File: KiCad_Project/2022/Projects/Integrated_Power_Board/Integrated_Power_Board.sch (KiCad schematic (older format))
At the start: 21 parts, among them J1 Conn_01x02, J2 Conn_01x02, J3 Conn_01x02, J4 Conn_01x02, J5 Conn_01x02, SW1 Switch_SW_SPST, SW2 SW_SPST, U1 OKL-T_6-W12N-C

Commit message: Kicadプロジェクトの整理
ファイルについて
各基板のプロジェクト・ライブラリ・PDF・DXF・自動配線用・発注ファイル
に分けました。
またライブラリのインポートに際してプロフェクトからの相対パスに変更したため環境を変更しても編集することができます。
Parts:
- BT1: footprint (none) -> Connector_JST:JST_VH_B2P-VH-B_1x02_P3.96mm_Vertical
- F1: footprint (none) -> herakuresu2022:fuse_socket
- MES1: footprint (none) -> herakuresu2022:voltage_counter
- SW1: symbol Integrated_Power_Board-cache:Switch_SW_SPST -> Integrated_Power_Board-rescue:Switch_SW_SPST-Integrated_Power_Board-cache
- SW2: footprint (none) -> herakuresu2022:2MS1T2B4M2QES
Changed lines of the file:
@@
 F 0 "SW2" V 6054 2948 50  0000 L CNN
 F 1 "SW_SPST" V 6145 2948 50  0000 L CNN
-F 2 "" H 6100 2850 50  0001 C CNN
+F 2 "herakuresu2022:2MS1T2B4M2QES" H 6100 2850 50  0001 C CNN
 F 3 "~" H 6100 2850 50  0001 C CNN
 	1    6100 2850
@@
 F 0 "BT1" H 1808 2596 50  0000 L CNN
 F 1 "Battery" H 1808 2505 50  0000 L CNN
-F 2 "" V 1700 2610 50  0001 C CNN
+F 2 "Connector_JST:JST_VH_B2P-VH-B_1x02_P3.96mm_Vertical" V 1700 2610 50  0001 C CNN
 F 3 "~" V 1700 2610 50  0001 C CNN
 	1    1700 2550
@@
 F 0 "F1" V 1803 2350 50  0000 C CNN
 F 1 "Fuse" V 1894 2350 50  0000 C CNN
-F 2 "" V 1930 2350 50  0001 C CNN
+F 2 "herakuresu2022:fuse_socket" V 1930 2350 50  0001 C CNN
 F 3 "~" H 2000 2350 50  0001 C CNN
 	1    2000 2350
@@
 $EndComp
 $Comp
-L Integrated_Power_Board-cache:Switch_SW_SPST SW1
+L Integrated_Power_Board-rescue:Switch_SW_SPST-Integrated_Power_Board-cache SW1
 U 1 1 61EC8A2A
 P 3300 2350
@@
 F 0 "MES1" H 3000 2450 50  0000 L CNN
 F 1 "Voltmeter_DC" H 2650 2250 50  0000 L CNN
-F 2 "" V 2900 2650 50  0001 C CNN
+F 2 "herakuresu2022:voltage_counter" V 2900 2650 50  0001 C CNN
 F 3 "~" V 2900 2650 50  0001 C CNN
 	1    2900 2550

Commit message: 電源系の設計の完了
ATtinyを使って電圧を測定してシリアルでメインマイコンに送信します
レベル変換についてはまだ考えてない
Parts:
- removed SW1: Switch_SW_SPST, symbol Integrated_Power_Board-rescue:Switch_SW_SPST-Integrated_Power_Board-cache
- added C1: CP, symbol Device:CP
- added D1: D_Shockley, symbol Device:D_Shockley
- added D2: LED, symbol Device:LED
- added J1: Conn_01x02, symbol Connector_Generic:Conn_01x02
- added R1, R2, R3: R, symbol Device:R
- added SW1: SW_SPST, herakuresu2022:2MS1T2B4M2QES, symbol Switch:SW_SPST
- added U1: ATtiny85-20PU, Package_DIP:DIP-8_W7.62mm, symbol MCU_Microchip_ATtiny:ATtiny85-20PU
- renumbered C1 to C2, C2 to C3, C3 to C4, D2 to D3, J1 to J2, J2 to J3, J3 to J4, J4 to J5, J5 to J6, R1 to R4, R2 to R5, R3 to R6, U1 to U2
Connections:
- net labels added: RX, TX
- wire segments 44 -> 61
- no-connect marks 1 -> 3
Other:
- moved on the sheet: BT1, F1, J2, J3, J4, MES1

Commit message: 進捗
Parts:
- C1, C2: footprint (none) -> Capacitor_THT:C_Radial_D16.0mm_H25.0mm_P7.50mm
- C3, C4: footprint (none) -> Capacitor_THT:C_Disc_D3.0mm_W1.6mm_P2.50mm
- D1: footprint (none) -> Diode_THT:D_DO-201AD_P12.70mm_Horizontal
- D2: footprint (none) -> LED_THT:LED_D3.0mm_Clear
- D3: footprint (none) -> Diode_THT:D_DO-41_SOD81_P7.62mm_Horizontal
- F1: footprint herakuresu2022:fuse_socket -> Library:fuse_socket
- FL1: footprint BNX016-01:FIL_BNX016-01 -> Library:FIL_BNX016-01
- J1: footprint (none) -> Connector_JST:JST_XH_B2B-XH-A_1x02_P2.50mm_Vertical
- MES1: footprint herakuresu2022:voltage_counter -> Library:voltage_counter
- R1, R2, R3, R4, R5, R6: footprint (none) -> Resistor_THT:R_Axial_DIN0207_L6.3mm_D2.5mm_P7.62mm_Horizontal
- RV2: footprint (none) -> Potentiometer_THT:Potentiometer_Bourns_3296W_Vertical
- SW1: footprint herakuresu2022:2MS1T2B4M2QES -> (none)
- SW2: footprint herakuresu2022:2MS1T2B4M2QES -> Library:toggleswitch
- U2: footprint OKL-T_6-W12N-C:DCDC-murata-6A -> Library:DCDC-murata-6A
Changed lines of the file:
@@
 F 0 "FL1" H 4500 2775 50  0000 C CNN
 F 1 "BNX025" H 4500 2684 50  0000 C CNN
-F 2 "BNX016-01:FIL_BNX016-01" H 4500 2250 50  0001 C CNN
+F 2 "Library:FIL_BNX016-01" H 4500 2250 50  0001 C CNN
 F 3 "https://www.murata.com/en-us/products/productdetail.aspx?cate=luNoiseSupprFilteBlockType&partno=BNX025H01%23" V 4475 2425 50  0001 C CNN
 	1    4500 2450
@@
 F 0 "C2" H 5418 2546 50  0000 L CNN
 F 1 "CP" H 5418 2455 50  0000 L CNN
-F 2 "" H 5338 2350 50  0001 C CNN
+F 2 "Capacitor_THT:C_Radial_D16.0mm_H25.0mm_P7.50mm" H 5338 2350 50  0001 C CNN
 F 3 "~" H 5300 2500 50  0001 C CNN
 	1    5300 2500
@@
 F 0 "D3" H 9350 2133 50  0000 C CNN
 F 1 "D" H 9350 2224 50  0000 C CNN
-F 2 "" H 9350 2350 50  0001 C CNN
+F 2 "Diode_THT:D_DO-41_SOD81_P7.62mm_Horizontal" H 9350 2350 50  0001 C CNN
 F 3 "~" H 9350 2350 50  0001 C CNN
 	1    9350 2350
@@
 F 0 "C4" H 8965 2696 50  0000 L CNN
 F 1 "C" H 8965 2605 50  0000 L CNN
-F 2 "" H 8888 2500 50  0001 C CNN
+F 2 "Capacitor_THT:C_Disc_D3.0mm_W1.6mm_P2.50mm" H 8888 2500 50  0001 C CNN
 F 3 "~" H 8850 2650 50  0001 C CNN
 	1    8850 2650
@@
 F 0 "C3" H 6015 2546 50  0000 L CNN
 F 1 "C" H 6015 2455 50  0000 L CNN
-F 2 "" H 5938 2350 50  0001 C CNN
+F 2 "Capacitor_THT:C_Disc_D3.0mm_W1.6mm_P2.50mm" H 5938 2350 50  0001 C CNN
 F 3 "~" H 5900 2500 50  0001 C CNN
 	1    5900 2500
@@
 F 0 "R4" H 6320 2596 50  0000 L CNN
 F 1 "R" H 6320 2505 50  0000 L CNN
-F 2 "" V 6180 2550 50  0001 C CNN
+F 2 "Resistor_THT:R_Axial_DIN0207_L6.3mm_D2.5mm_P7.62mm_Horizontal" V 6180 2550 50  0001 C CNN
 F 3 "~" H 6250 2550 50  0001 C CNN
 	1    6250 2550
@@
 F 0 "R6" H 9220 2696 50  0000 L CNN
 F 1 "R" H 9220 2605 50  0000 L CNN
-F 2 "" V 9080 2650 50  0001 C CNN
+F 2 "Resistor_THT:R_Axial_DIN0207_L6.3mm_D2.5mm_P7.62mm_Horizontal" V 9080 2650 50  0001 C CNN
 F 3 "~" H 9150 2650 50  0001 C CNN
 	1    9150 2650
@@
 F 0 "RV2" V 8175 2725 50  0000 R CNN
 F 1 "R_POT_TRIM_US" V 8450 2950 50  0000 R CNN
-F 2 "" H 8250 2650 50  0001 C CNN
+F 2 "Potentiometer_THT:Potentiometer_Bourns_3296W_Vertical" H 8250 2650 50  0001 C CNN
 F 3 "~" H 8250 2650 50  0001 C CNN
 	1    8250 2650
@@
 F 0 "R5" H 8670 2846 50  0000 L CNN
 F 1 "R" H 8670 2755 50  0000 L CNN
-F 2 "" V 8530 2800 50  0001 C CNN
+F 2 "Resistor_THT:R_Axial_DIN0207_L6.3mm_D2.5mm_P7.62mm_Horizontal" V 8530 2800 50  0001 C CNN
 F 3 "~" H 8600 2800 50  0001 C CNN
 	1    8600 2800
@@
 F 0 "F1" V 1678 2350 50  0000 C CNN
 F 1 "Fuse" V 1769 2350 50  0000 C CNN
-F 2 "herakuresu2022:fuse_socket" V 1805 2350 50  0001 C CNN
+F 2 "Library:fuse_socket" V 1805 2350 50  0001 C CNN
 F 3 "~" H 1875 2350 50  0001 C CNN
 	1    1875 2350
@@
 F 0 "MES1" H 2875 2450 50  0000 L CNN
 F 1 "Voltmeter_DC" H 2525 2250 50  0000 L CNN
-F 2 "herakuresu2022:voltage_counter" V 2775 2650 50  0001 C CNN
+F 2 "Library:voltage_counter" V 2775 2650 50  0001 C CNN
 F 3 "~" V 2775 2650 50  0001 C CNN
 	1    2775 2550
@@
 F 0 "SW2" V 6054 2948 50  0000 L CNN
 F 1 "SW_SPST" V 6145 2948 50  0000 L CNN
-F 2 "herakuresu2022:2MS1T2B4M2QES" H 6100 2850 50  0001 C CNN
+F 2 "Library:toggleswitch" H 6100 2850 50  0001 C CNN
 F 3 "~" H 6100 2850 50  0001 C CNN
 	1    6100 2850
@@
 F 0 "U2" H 7200 3215 50  0000 C CNN
 F 1 "OKL-T_6-W12N-C" H 7200 3124 50  0000 C CNN
-F 2 "OKL-T_6-W12N-C:DCDC-murata-6A" H 6750 3100 50  0001 L BNN
+F 2 "Library:DCDC-murata-6A" H 6750 3100 50  0001 L BNN
 F 3 "" H 7200 2650 50  0001 L BNN
 	1    7200 2650
@@
 F 0 "SW1" V 3129 2448 50  0000 L CNN
 F 1 "SW_SPST" V 3220 2448 50  0000 L CNN
-F 2 "herakuresu2022:2MS1T2B4M2QES" H 3175 2350 50  0001 C CNN
+F 2 "" H 3175 2350 50  0001 C CNN
 F 3 "~" H 3175 2350 50  0001 C CNN
 	1    3175 2350
@@
 F 0 "D1" V 2054 2630 50  0000 L CNN
 F 1 "D_Shockley" V 2145 2630 50  0000 L CNN
-F 2 "" H 2100 2550 50  0001 C CNN
+F 2 "Diode_THT:D_DO-201AD_P12.70mm_Horizontal" H 2100 2550 50  0001 C CNN
 F 3 "~" H 2100 2550 50  0001 C CNN
 	1    2100 2550
@@
 F 0 "C1" H 3593 2596 50  0000 L CNN
 F 1 "CP" H 3593 2505 50  0000 L CNN
-F 2 "" H 3513 2400 50  0001 C CNN
+F 2 "Capacitor_THT:C_Radial_D16.0mm_H25.0mm_P7.50mm" H 3513 2400 50  0001 C CNN
 F 3 "~" H 3475 2550 50  0001 C CNN
 	1    3475 2550
@@
 F 0 "R2" H 4195 3821 50  0000 L CNN
 F 1 "R" H 4195 3730 50  0000 L CNN
-F 2 "" V 4055 3775 50  0001 C CNN
+F 2 "Resistor_THT:R_Axial_DIN0207_L6.3mm_D2.5mm_P7.62mm_Horizontal" V 4055 3775 50  0001 C CNN
 F 3 "~" H 4125 3775 50  0001 C CNN
 	1    4125 3775
@@
 F 0 "R3" H 4195 4121 50  0000 L CNN
 F 1 "R" H 4195 4030 50  0000 L CNN
-F 2 "" V 4055 4075 50  0001 C CNN
+F 2 "Resistor_THT:R_Axial_DIN0207_L6.3mm_D2.5mm_P7.62mm_Horizontal" V 4055 4075 50  0001 C CNN
 F 3 "~" H 4125 4075 50  0001 C CNN
 	1    4125 4075
@@
 F 0 "J1" H 3430 3717 50  0000 L CNN
 F 1 "Conn_01x02" H 3430 3626 50  0000 L CNN
-F 2 "" H 3350 3725 50  0001 C CNN
+F 2 "Connector_JST:JST_XH_B2B-XH-A_1x02_P2.50mm_Vertical" H 3350 3725 50  0001 C CNN
 F 3 "~" H 3350 3725 50  0001 C CNN
 	1    3350 3725
@@
 F 0 "D2" V 3489 4432 50  0000 R CNN
 F 1 "LED" V 3398 4432 50  0000 R CNN
-F 2 "" H 3450 4550 50  0001 C CNN
+F 2 "LED_THT:LED_D3.0mm_Clear" H 3450 4550 50  0001 C CNN
 F 3 "~" H 3450 4550 50  0001 C CNN
 	1    3450 4550
@@
 F 0 "R1" H 3520 4246 50  0000 L CNN
 F 1 "R" H 3520 4155 50  0000 L CNN
-F 2 "" V 3380 4200 50  0001 C CNN
+F 2 "Resistor_THT:R_Axial_DIN0207_L6.3mm_D2.5mm_P7.62mm_Horizontal" V 3380 4200 50  0001 C CNN
 F 3 "~" H 3450 4200 50  0001 C CNN
 	1    3450 4200

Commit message: 部品の配置
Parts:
- added C5: C, Capacitor_THT:C_Disc_D3.0mm_W1.6mm_P2.50mm, symbol Device:C
- RV1: footprint (none) -> Varistor:RV_Disc_D9mm_W3.3mm_P5mm
- SW1: footprint (none) -> Library:DS-850k
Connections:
- net +5V: now also C5.1
- net GND: no longer D2.1 (K)
- net GND1: now also D2.1 (K), C5.2
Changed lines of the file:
@@
 F 0 "RV1" H 3753 2546 50  0000 L CNN
 F 1 "Varistor" H 3753 2455 50  0000 L CNN
-F 2 "" V 3580 2500 50  0001 C CNN
+F 2 "Varistor:RV_Disc_D9mm_W3.3mm_P5mm" V 3580 2500 50  0001 C CNN
 F 3 "~" H 3650 2500 50  0001 C CNN
 	1    3650 2500
@@
 F 0 "SW1" V 3129 2448 50  0000 L CNN
 F 1 "SW_SPST" V 3220 2448 50  0000 L CNN
-F 2 "" H 3175 2350 50  0001 C CNN
+F 2 "Library:DS-850k" H 3175 2350 50  0001 C CNN
 F 3 "~" H 3175 2350 50  0001 C CNN
 	1    3175 2350
@@
 Wire Wire Line
 	3450 4025 2925 4025
-$Comp
-L power:GND #PWR04
-U 1 1 62041296
+Wire Wire Line
+	3450 4750 3450 4700
+Wire Wire Line
+	2325 4600 2325 4625
+Wire Wire Line
+	1150 3425 2325 3425
+Connection ~ 2325 3425
+Connection ~ 2325 4625
+Wire Wire Line
+	2325 4625 1150 4625
+$Comp
+L power:GND1 #PWR04
+U 1 1 62031C83
 P 3450 4750
 F 0 "#PWR04" H 3450 4500 50  0001 C CNN
-F 1 "GND" H 3455 4577 50  0000 C CNN
+F 1 "GND1" H 3455 4577 50  0000 C CNN
 F 2 "" H 3450 4750 50  0001 C CNN
 F 3 "" H 3450 4750 50  0001 C CNN
@@
 	1    0    0    -1
 $EndComp
-Wire Wire Line
-	3450 4750 3450 4700
+$Comp
+L Device:C C5
+U 1 1 620440A9
+P 1150 3975
+F 0 "C5" H 1265 4021 50  0000 L CNN
+F 1 "C" H 1265 3930 50  0000 L CNN
+F 2 "Capacitor_THT:C_Disc_D3.0mm_W1.6mm_P2.50mm" H 1188 3825 50  0001 C CNN
+F 3 "~" H 1150 3975 50  0001 C CNN
+	1    1150 3975
+	1    0    0    -1
+$EndComp
+Wire Wire Line
+	1150 3825 1150 3425
+Wire Wire Line
+	1150 4125 1150 4625
 $EndSCHEMATC

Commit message: 統合電源基板の設計の完了
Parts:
- removed J4: Conn_01x02, Connector_JST:JST_XH_B2B-XH-A_1x02_P2.50mm_Vertical, symbol Connector_Generic:Conn_01x02
- C3, C4: footprint Capacitor_THT:C_Disc_D3.0mm_W1.6mm_P2.50mm -> Capacitor_THT:C_Disc_D4.3mm_W1.9mm_P5.00mm
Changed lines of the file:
@@
 F 0 "C4" H 8965 2696 50  0000 L CNN
 F 1 "C" H 8965 2605 50  0000 L CNN
-F 2 "Capacitor_THT:C_Disc_D3.0mm_W1.6mm_P2.50mm" H 8888 2500 50  0001 C CNN
+F 2 "Capacitor_THT:C_Disc_D4.3mm_W1.9mm_P5.00mm" H 8888 2500 50  0001 C CNN
 F 3 "~" H 8850 2650 50  0001 C CNN
 	1    8850 2650
@@
 F 0 "C3" H 6015 2546 50  0000 L CNN
 F 1 "C" H 6015 2455 50  0000 L CNN
-F 2 "Capacitor_THT:C_Disc_D3.0mm_W1.6mm_P2.50mm" H 5938 2350 50  0001 C CNN
+F 2 "Capacitor_THT:C_Disc_D4.3mm_W1.9mm_P5.00mm" H 5938 2350 50  0001 C CNN
 F 3 "~" H 5900 2500 50  0001 C CNN
 	1    5900 2500
@@
 	1    0    0    -1
 $EndComp
-$Comp
-L Connector_Generic:Conn_01x02 J4
-U 1 1 61EEE7BE
-P 7350 3625
-F 0 "J4" V 7314 3437 50  0000 R CNN
-F 1 "Conn_01x02" V 7223 3437 50  0000 R CNN
-F 2 "Connector_JST:JST_XH_B2B-XH-A_1x02_P2.50mm_Vertical" H 7350 3625 50  0001 C CNN
-F 3 "~" H 7350 3625 50  0001 C CNN
-	1    7350 3625
-	0    -1   -1   0
-$EndComp
-$Comp
-L power:+12V #PWR011
-U 1 1 61EEE7C4
-P 7350 3825
-F 0 "#PWR011" H 7350 3675 50  0001 C CNN
-F 1 "+12V" H 7425 4000 50  0000 C CNN
-F 2 "" H 7350 3825 50  0001 C CNN
-F 3 "" H 7350 3825 50  0001 C CNN
-	1    7350 3825
-	-1   0    0    1
-$EndComp
-$Comp
-L power:GND #PWR012
-U 1 1 61EEE7CA
-P 7450 3825
-F 0 "#PWR012" H 7450 3575 50  0001 C CNN
-F 1 "GND" H 7550 3650 50  0000 C CNN
-F 2 "" H 7450 3825 50  0001 C CNN
-F 3 "" H 7450 3825 50  0001 C CNN
-	1    7450 3825
-	1    0    0    -1
-$EndComp

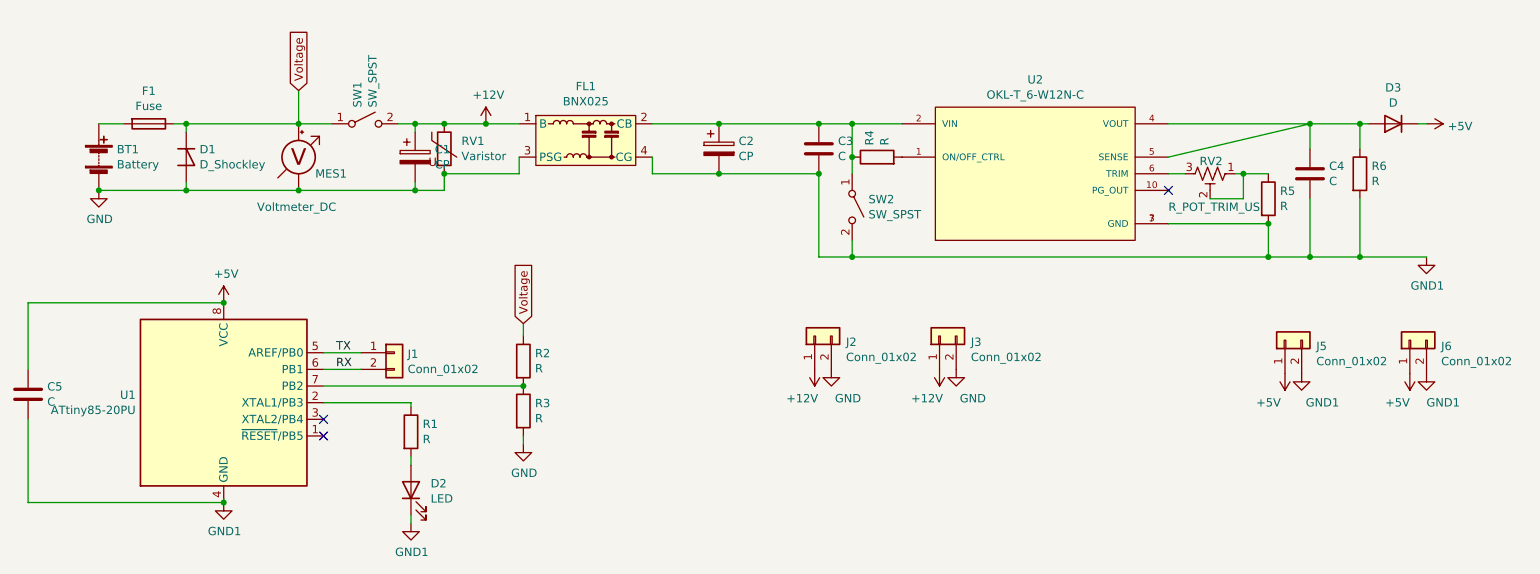
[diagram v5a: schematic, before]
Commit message: 設計図資料の更新と発注用ファイルの作成
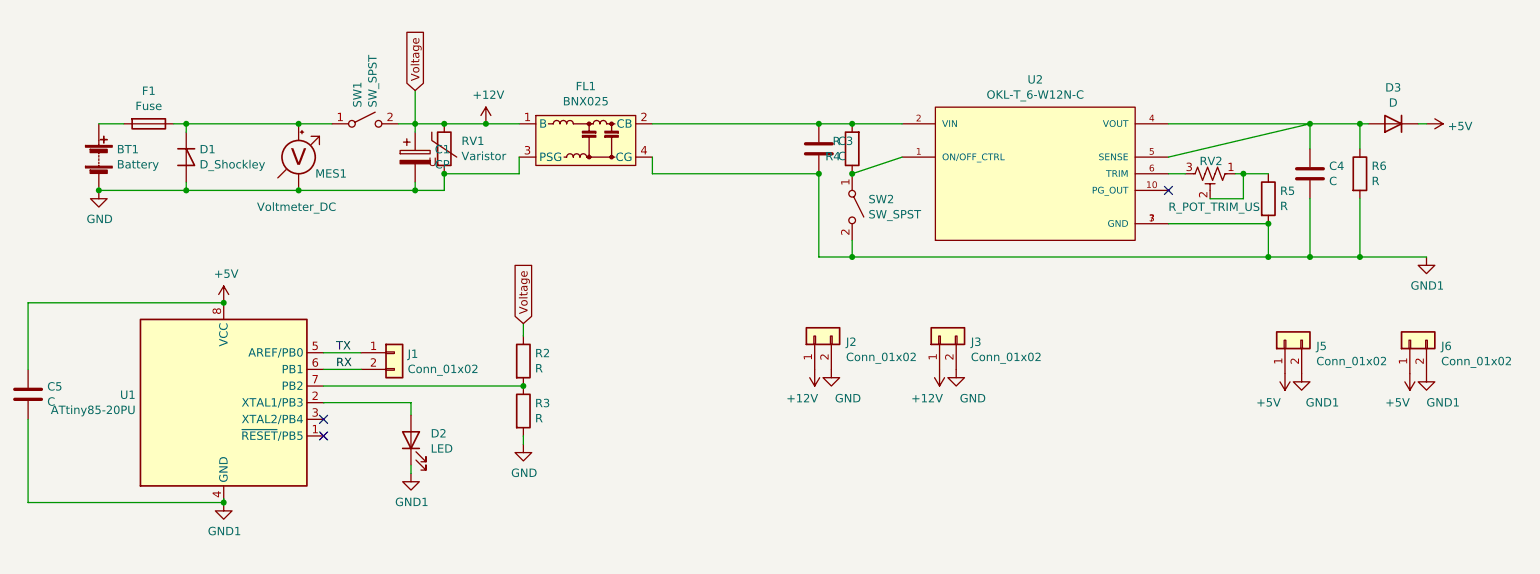
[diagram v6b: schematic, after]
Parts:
- removed C2: CP, Capacitor_THT:C_Radial_D16.0mm_H25.0mm_P7.50mm, symbol Device:CP
- removed R1: R, Resistor_THT:R_Axial_DIN0207_L6.3mm_D2.5mm_P7.62mm_Horizontal, symbol Device:R
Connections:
- net +12V: now also R2.1
- net at C3.1, FL1.2 (CB), U2.2 (VIN): now also R4.2; no longer R4.1, SW2.1 (A)
- net at U2.1 (ON/OFF_CTRL): now also R4.1, SW2.1 (A); no longer R4.2
- net at U1.2 (XTAL1/PB3): now also D2.2 (A)
- net Voltage: no longer names the net of D1.1 (K), F1.1, MES1.2 (+), SW1.1 (A)
- net Voltage: no longer R2.1
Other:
- moved on the sheet: D2, R4
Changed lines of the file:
@@
 	1    0    0    -1
 $EndComp
-$Comp
-L Device:CP C2
-U 1 1 61E9D1C6
-P 5300 2500
-F 0 "C2" H 5418 2546 50  0000 L CNN
-F 1 "CP" H 5418 2455 50  0000 L CNN
-F 2 "Capacitor_THT:C_Radial_D16.0mm_H25.0mm_P7.50mm" H 5338 2350 50  0001 C CNN
-F 3 "~" H 5300 2500 50  0001 C CNN
-	1    5300 2500
-	1    0    0    -1
-$EndComp
-Wire Wire Line
-	4900 2350 5300 2350
 Wire Wire Line
 	4900 2550 4900 2650
-Wire Wire Line
-	4900 2650 5300 2650
-Connection ~ 5300 2350
 $Comp
 L Device:D D3
@@
 $EndComp
 Wire Wire Line
-	5300 2350 5900 2350
-Connection ~ 5900 2350
-Wire Wire Line
-	5900 2350 6100 2350
-Wire Wire Line
 	5900 2650 5900 3150
-Wire Wire Line
-	5300 2650 5900 2650
-Connection ~ 5300 2650
 Connection ~ 5900 2650
-$Comp
-L Device:R R4
-U 1 1 61ED432C
-P 6250 2550
-F 0 "R4" H 6320 2596 50  0000 L CNN
-F 1 "R" H 6320 2505 50  0000 L CNN
-F 2 "Resistor_THT:R_Axial_DIN0207_L6.3mm_D2.5mm_P7.62mm_Horizontal" V 6180 2550 50  0001 C CNN
-F 3 "~" H 6250 2550 50  0001 C CNN
-	1    6250 2550
-	0    -1   -1   0
-$EndComp
-Wire Wire Line
-	6100 2550 6100 2350
-Connection ~ 6100 2350
-Wire Wire Line
-	6100 2350 6400 2350
 NoConn ~ 8000 2750
 Wire Wire Line
@@
 Wire Wire Line
 	6100 3150 8600 3150
-Wire Wire Line
-	6100 2650 6100 2550
-Connection ~ 6100 2550
 Wire Wire Line
 	8850 2350 8850 2500
@@
 Connection ~ 3650 2350
 Connection ~ 1575 2750
-Text GLabel 2775 2150 1    50   Input ~ 0
+Text GLabel 3475 2150 1    50   Input ~ 0
 Voltage
 Wire Wire Line
-	2775 2150 2775 2350
+	3475 2150 3475 2350
 $Comp
 L Connector_Generic:Conn_01x02 J2
@@
 $EndComp
 $Comp
-L Converter_DCDC:OKL-T_6-W12N-C U2
-U 1 1 61EADD40
-P 7200 2650
-F 0 "U2" H 7200 3215 50  0000 C CNN
-F 1 "OKL-T_6-W12N-C" H 7200 3124 50  0000 C CNN
-F 2 "Library:DCDC-murata-6A" H 6750 3100 50  0001 L BNN
-F 3 "" H 7200 2650 50  0001 L BNN
-	1    7200 2650
-	1    0    0    -1
-$EndComp
-$Comp
 L Switch:SW_SPST SW1
 U 1 1 62001AB7
@@
 L Device:LED D2
 U 1 1 62036027
-P 3450 4550
-F 0 "D2" V 3489 4432 50  0000 R CNN
-F 1 "LED" V 3398 4432 50  0000 R CNN
-F 2 "LED_THT:LED_D3.0mm_Clear" H 3450 4550 50  0001 C CNN
-F 3 "~" H 3450 4550 50  0001 C CNN
-	1    3450 4550
+P 3450 4250
+F 0 "D2" V 3489 4132 50  0000 R CNN
+F 1 "LED" V 3398 4132 50  0000 R CNN
+F 2 "LED_THT:LED_D3.0mm_Clear" H 3450 4250 50  0001 C CNN
+F 3 "~" H 3450 4250 50  0001 C CNN
+	1    3450 4250
 	0    -1   -1   0
 $EndComp
-$Comp
-L Device:R R1
-U 1 1 6203AED7
-P 3450 4200
-F 0 "R1" H 3520 4246 50  0000 L CNN
-F 1 "R" H 3520 4155 50  0000 L CNN
-F 2 "Resistor_THT:R_Axial_DIN0207_L6.3mm_D2.5mm_P7.62mm_Horizontal" V 3380 4200 50  0001 C CNN
-F 3 "~" H 3450 4200 50  0001 C CNN
-	1    3450 4200
-	1    0    0    -1
-$EndComp
 Wire Wire Line
 	4125 4275 4125 4225
 Wire Wire Line
-	3450 4400 3450 4350
-Wire Wire Line
-	3450 4050 3450 4025
-Wire Wire Line
 	3450 4025 2925 4025
 Wire Wire Line
-	3450 4750 3450 4700
+	3450 4450 3450 4400
 Wire Wire Line
 	2325 4600 2325 4625
@@
 L power:GND1 #PWR04
 U 1 1 62031C83
-P 3450 4750
-F 0 "#PWR04" H 3450 4500 50  0001 C CNN
-F 1 "GND1" H 3455 4577 50  0000 C CNN
-F 2 "" H 3450 4750 50  0001 C CNN
-F 3 "" H 3450 4750 50  0001 C CNN
-	1    3450 4750
+P 3450 4450
+F 0 "#PWR04" H 3450 4200 50  0001 C CNN
+F 1 "GND1" H 3455 4277 50  0000 C CNN
+F 2 "" H 3450 4450 50  0001 C CNN
+F 3 "" H 3450 4450 50  0001 C CNN
+	1    3450 4450
 	1    0    0    -1
 $EndComp
@@
 Wire Wire Line
 	1150 4125 1150 4625
+Wire Wire Line
+	4900 2350 5900 2350
+Wire Wire Line
+	4900 2650 5900 2650
+Wire Wire Line
+	3450 4025 3450 4100
+Connection ~ 5900 2350
+Wire Wire Line
+	5900 2350 6100 2350
+$Comp
+L Converter_DCDC:OKL-T_6-W12N-C U2
+U 1 1 61EADD40
+P 7200 2650
+F 0 "U2" H 7200 3215 50  0000 C CNN
+F 1 "OKL-T_6-W12N-C" H 7200 3124 50  0000 C CNN
+F 2 "Library:DCDC-murata-6A" H 6750 3100 50  0001 L BNN
+F 3 "" H 7200 2650 50  0001 L BNN
+	1    7200 2650
+	1    0    0    -1
+$EndComp
+$Comp
+L Device:R R4
+U 1 1 61ED432C
+P 6100 2500
+F 0 "R4" H 6170 2546 50  0000 L CNN
+F 1 "R" H 6170 2455 50  0000 L CNN
+F 2 "Resistor_THT:R_Axial_DIN0207_L6.3mm_D2.5mm_P7.62mm_Horizontal" V 6030 2500 50  0001 C CNN
+F 3 "~" H 6100 2500 50  0001 C CNN
+	1    6100 2500
+	-1   0    0    1
+$EndComp
+Connection ~ 6100 2350
+Wire Wire Line
+	6100 2350 6400 2350
+Wire Wire Line
+	6100 2650 6400 2550
+Connection ~ 6100 2650
 $EndSCHEMATC
